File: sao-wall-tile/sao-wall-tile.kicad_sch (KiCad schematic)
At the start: 22 parts, among them J1 Power In, J2 Power Out, J3 Power Out, J4 Conn_02x03_Odd_Even, J5 Conn_02x03_Odd_Even, J6 Conn_02x03_Odd_Even, J7 Conn_02x03_Odd_Even, U1 LM2594M-3.3

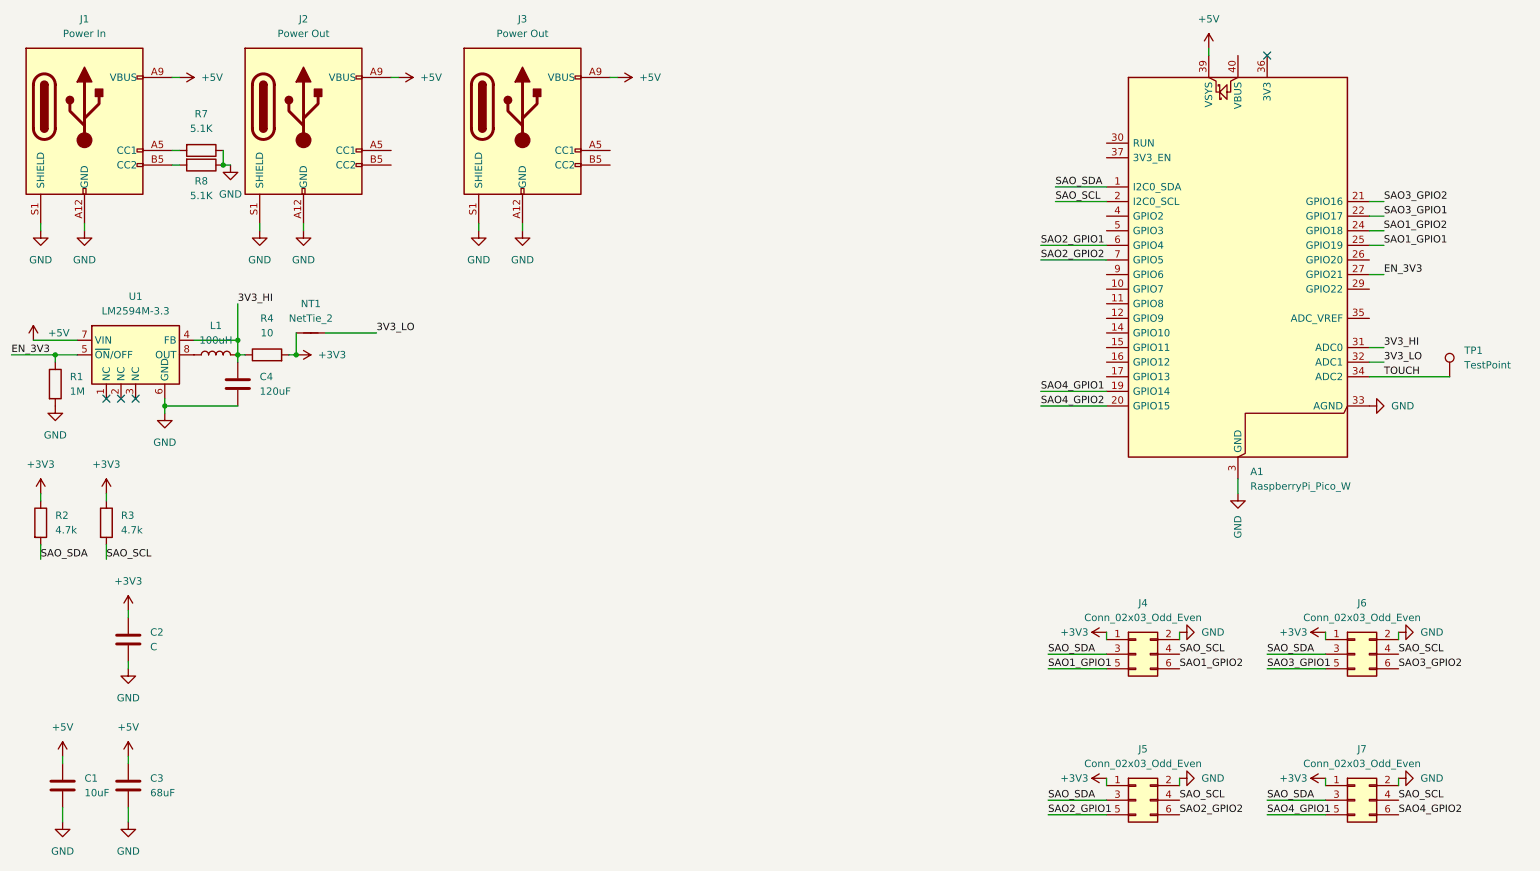
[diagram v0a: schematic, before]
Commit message: Add README, clean up schematic and layout
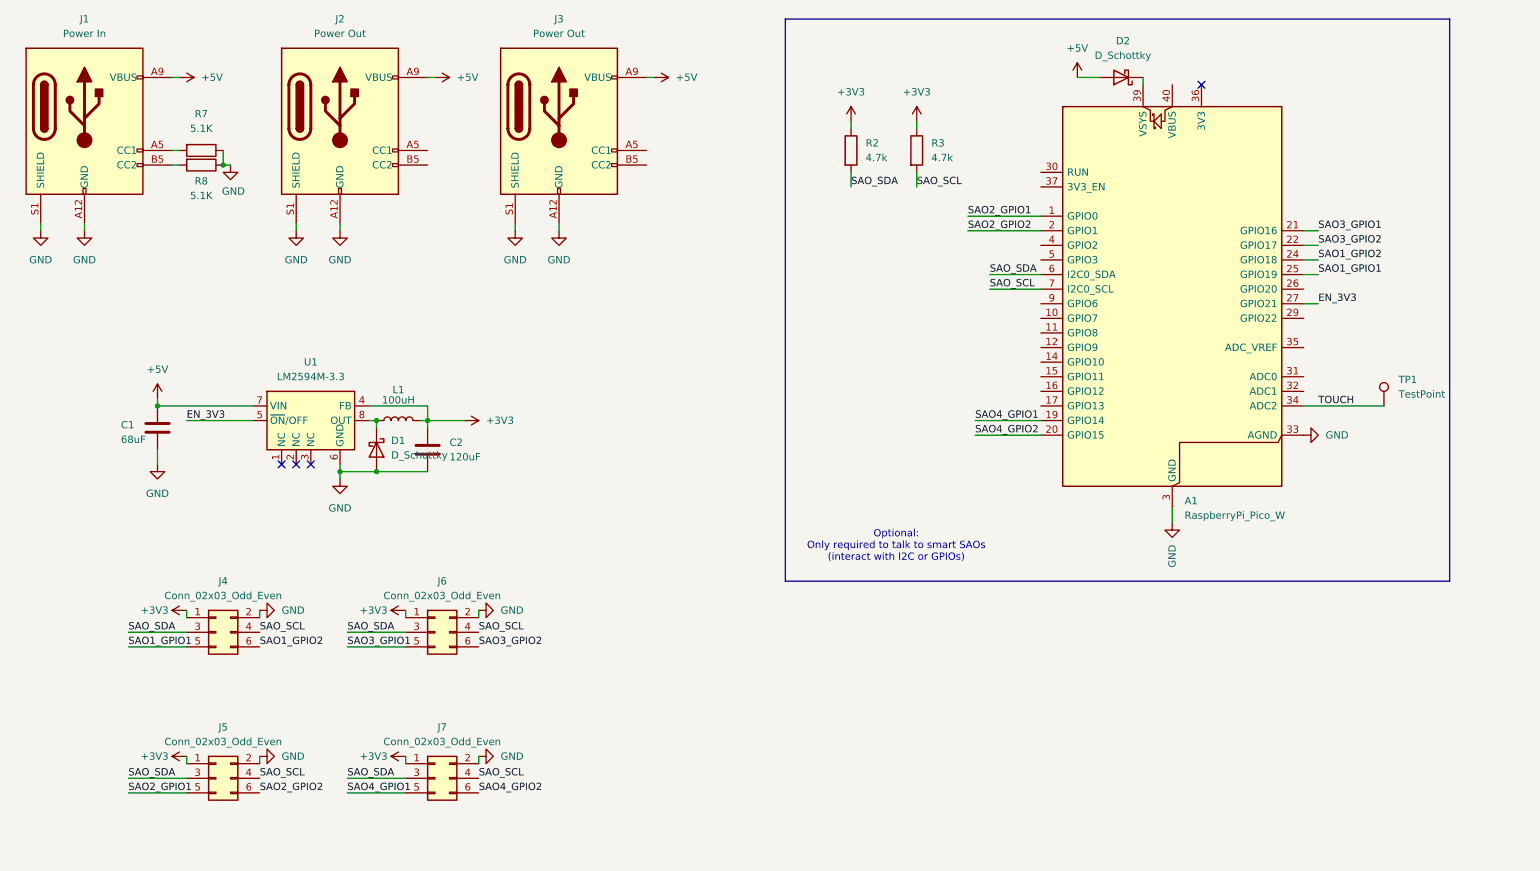
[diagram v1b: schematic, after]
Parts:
- removed C1: 10uF, Capacitor_SMD:C_0603_1608Metric, symbol Device:C
- removed C2: C, Capacitor_SMD:C_0603_1608Metric, symbol Device:C
- removed NT1: NetTie_2, NetTie:NetTie-2_SMD_Pad0.5mm, symbol Device:NetTie_2
- removed R1: 1M, Resistor_SMD:R_0603_1608Metric_Pad0.98x0.95mm_HandSolder, symbol Device:R
- removed R4: 10, Resistor_SMD:R_0603_1608Metric_Pad0.98x0.95mm_HandSolder, symbol Device:R
- added D1, D2: D_Schottky, Diode_SMD:D_0603_1608Metric_Pad1.05x0.95mm_HandSolder, symbol Device:D_Schottky
- renumbered C3 to C1, C4 to C2
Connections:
- net +3V3: now also C2.1, L1.2, U1.4 (FB)
- net +5V: now also D2.2 (A); no longer A1.39 (VSYS)
- net GND: now also D1.2 (A)
- net SAO2_GPIO1: now also A1.1 (GPIO0); no longer A1.6 (GPIO4)
- net SAO2_GPIO2: now also A1.2 (GPIO1); no longer A1.7 (GPIO5)
- net SAO3_GPIO1: now also A1.21 (GPIO16); no longer A1.22 (GPIO17)
- net SAO3_GPIO2: now also A1.22 (GPIO17); no longer A1.21 (GPIO16)
- net SAO_SCL: now also A1.7 (GPIO5); no longer A1.2 (GPIO1)
- net SAO_SDA: now also A1.6 (GPIO4); no longer A1.1 (GPIO0)
- net at L1.1, U1.8 (OUT): now also D1.1 (K)
- removed net 3V3_HI: A1.31 (GPIO26_ADC0), C2.1, L1.2, U1.4 (FB)
- net 3V3_LO: no longer names the net of A1.32 (GPIO27_ADC1)
- new net: A1.39 (VSYS), D2.1 (K)
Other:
- note added: "Optional: Only required to talk to smart SAOs (interact with I2C or GPIOs)"
- moved on the sheet: A1, C1, C2, J2, J3, J4, J5, J6, J7, L1, R2, R3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

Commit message: Update from review feedback
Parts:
- C1, C2: footprint Capacitor_SMD:C_0603_1608Metric -> Capacitor_SMD:C_0805_2012Metric_Pad1.18x1.45mm_HandSolder
- D1, D2: footprint Diode_SMD:D_0603_1608Metric_Pad1.05x0.95mm_HandSolder -> Diode_SMD:D_0805_2012Metric_Pad1.15x1.40mm_HandSolder
- L1: footprint Inductor_SMD:L_0603_1608Metric -> Inductor_SMD:L_0805_2012Metric_Pad1.05x1.20mm_HandSolder
- R2, R3, R7, R8: footprint Resistor_SMD:R_0603_1608Metric_Pad0.98x0.95mm_HandSolder -> Resistor_SMD:R_0805_2012Metric_Pad1.20x1.40mm_HandSolder
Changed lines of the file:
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@@
 	(wire
 		(pts
+			(xy 248.92 92.71) (xy 247.65 92.71)
+		)
+		(stroke
+			(width 0)
+			(type default)
+		)
+	)
+	(wire
+		(pts
 			(xy 86.36 99.06) (xy 95.25 99.06)
 		)
@@
 			)
 		)
-		(property "Footprint" "Resistor_SMD:R_0603_1608Metric_Pad0.98x0.95mm_HandSolder"
+		(property "Footprint" "Resistor_SMD:R_0805_2012Metric_Pad1.20x1.40mm_HandSolder"
 			(at 55.88 43.942 90)
 			(effects
@@
 			)
 		)
-		(property "Footprint" "Resistor_SMD:R_0603_1608Metric_Pad0.98x0.95mm_HandSolder"
+		(property "Footprint" "Resistor_SMD:R_0805_2012Metric_Pad1.20x1.40mm_HandSolder"
 			(at 178.562 43.18 90)
 			(effects
@@
 			)
 		)
-		(property "Footprint" "Capacitor_SMD:C_0603_1608Metric"
+		(property "Footprint" "Capacitor_SMD:C_0805_2012Metric_Pad1.18x1.45mm_HandSolder"
 			(at 49.2252 95.25 0)
 			(effects
@@
 			)
 		)
-		(property "Footprint" "Resistor_SMD:R_0603_1608Metric_Pad0.98x0.95mm_HandSolder"
+		(property "Footprint" "Resistor_SMD:R_0805_2012Metric_Pad1.20x1.40mm_HandSolder"
 			(at 167.132 43.18 90)
 			(effects
@@
 			)
 		)
-		(property "Footprint" "Inductor_SMD:L_0603_1608Metric"
+		(property "Footprint" "Inductor_SMD:L_0805_2012Metric_Pad1.05x1.20mm_HandSolder"
 			(at 90.17 90.17 0)
 			(effects
@@
 			)
 		)
-		(property "Footprint" "Diode_SMD:D_0603_1608Metric_Pad1.05x0.95mm_HandSolder"
+		(property "Footprint" "Diode_SMD:D_0805_2012Metric_Pad1.15x1.40mm_HandSolder"
 			(at 215.9 30.48 0)
 			(effects
@@
 			)
 		)
-		(property "Footprint" "Resistor_SMD:R_0603_1608Metric_Pad0.98x0.95mm_HandSolder"
+		(property "Footprint" "Resistor_SMD:R_0805_2012Metric_Pad1.20x1.40mm_HandSolder"
 			(at 55.88 41.402 90)
 			(effects
@@
 	(symbol
 		(lib_id "power:GND")
-		(at 247.65 92.71 90)
+		(at 248.92 92.71 90)
 		(unit 1)
 		(exclude_from_sim no)
@@
 		(dnp no)
 		(property "Reference" "#PWR016"
-			(at 254 92.71 0)
+			(at 255.27 92.71 0)
 			(effects
 				(font
@@
 		)
 		(property "Value" "GND"
-			(at 251.46 92.7101 90)
+			(at 252.73 92.7101 90)
 			(effects
 				(font
@@
 		)
 		(property "Footprint" ""
-			(at 247.65 92.71 0)
+			(at 248.92 92.71 0)
 			(effects
 				(font
@@
 		)
 		(property "Datasheet" ""
-			(at 247.65 92.71 0)
+			(at 248.92 92.71 0)
 			(effects
 				(font
@@
 		)
 		(property "Description" "Power symbol creates a global label with name \"GND\" , ground"
-			(at 247.65 92.71 0)
+			(at 248.92 92.71 0)
 			(effects
 				(font
@@
 			)
 		)
-		(property "Footprint" "Capacitor_SMD:C_0603_1608Metric"
+		(property "Footprint" "Capacitor_SMD:C_0805_2012Metric_Pad1.18x1.45mm_HandSolder"
 			(at 96.2152 99.06 0)
 			(effects
@@
 			)
 		)
-		(property "Footprint" "Diode_SMD:D_0603_1608Metric_Pad1.05x0.95mm_HandSolder"
+		(property "Footprint" "Diode_SMD:D_0805_2012Metric_Pad1.15x1.40mm_HandSolder"
 			(at 86.36 95.25 0)
 			(effects

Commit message: Updates from picking components on digikey
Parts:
- C1: footprint Capacitor_SMD:C_0805_2012Metric_Pad1.18x1.45mm_HandSolder -> Capacitor_SMD:C_Elec_5x5.8
- C2: footprint Capacitor_SMD:C_0805_2012Metric_Pad1.18x1.45mm_HandSolder -> Capacitor_SMD:C_Elec_8x10.2
- D1: footprint Diode_SMD:D_0805_2012Metric_Pad1.15x1.40mm_HandSolder -> Diode_SMD:D_SOD-123
- L1: value 100uH -> 47uH; footprint Inductor_SMD:L_0805_2012Metric_Pad1.05x1.20mm_HandSolder -> Inductor_SMD:L_Taiyo-Yuden_NR-60xx_HandSoldering
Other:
- moved on the sheet: C2
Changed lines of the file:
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@@
 	)
 	(junction
-		(at 86.36 90.17)
+		(at 102.87 90.17)
 		(diameter 0)
 		(color 0 0 0 0)
 	)
 	(junction
-		(at 48.26 87.63)
+		(at 86.36 90.17)
 		(diameter 0)
 		(color 0 0 0 0)
 	)
 	(junction
-		(at 95.25 90.17)
+		(at 48.26 87.63)
 		(diameter 0)
 		(color 0 0 0 0)
@@
 	(wire
 		(pts
-			(xy 86.36 99.06) (xy 95.25 99.06)
+			(xy 86.36 99.06) (xy 102.87 99.06)
 		)
 		(stroke
@@
 	(wire
 		(pts
-			(xy 95.25 87.63) (xy 95.25 90.17)
+			(xy 102.87 87.63) (xy 102.87 90.17)
 		)
 		(stroke
@@
 	(wire
 		(pts
-			(xy 95.25 90.17) (xy 93.98 90.17)
+			(xy 102.87 90.17) (xy 93.98 90.17)
 		)
 		(stroke
@@
 	(wire
 		(pts
-			(xy 95.25 91.44) (xy 95.25 90.17)
+			(xy 102.87 91.44) (xy 102.87 90.17)
 		)
 		(stroke
@@
 	(wire
 		(pts
-			(xy 85.09 87.63) (xy 95.25 87.63)
+			(xy 85.09 87.63) (xy 102.87 87.63)
 		)
 		(stroke
@@
 	(wire
 		(pts
-			(xy 101.6 90.17) (xy 95.25 90.17)
+			(xy 110.49 90.17) (xy 102.87 90.17)
 		)
 		(stroke
@@
 	(symbol
 		(lib_id "power:VCC")
-		(at 101.6 90.17 270)
+		(at 110.49 90.17 270)
 		(unit 1)
 		(exclude_from_sim no)
@@
 		(fields_autoplaced yes)
 		(property "Reference" "#PWR025"
-			(at 97.79 90.17 0)
+			(at 106.68 90.17 0)
 			(effects
 				(font
@@
 		)
 		(property "Value" "+3V3"
-			(at 105.41 90.1699 90)
+			(at 114.3 90.1699 90)
 			(effects
 				(font
@@
 		)
 		(property "Footprint" ""
-			(at 101.6 90.17 0)
+			(at 110.49 90.17 0)
 			(effects
 				(font
@@
 		)
 		(property "Datasheet" ""
-			(at 101.6 90.17 0)
+			(at 110.49 90.17 0)
 			(effects
 				(font
@@
 		)
 		(property "Description" "Power symbol creates a global label with name \"VCC\""
-			(at 101.6 90.17 0)
+			(at 110.49 90.17 0)
 			(effects
 				(font
@@
 			)
 		)
-		(property "Footprint" "Capacitor_SMD:C_0805_2012Metric_Pad1.18x1.45mm_HandSolder"
+		(property "Footprint" "Capacitor_SMD:C_Elec_5x5.8"
 			(at 49.2252 95.25 0)
 			(effects
@@
 			)
 		)
-		(property "Value" "100uH"
+		(property "Value" "47uH"
 			(at 90.17 86.614 90)
 			(effects
@@
 			)
 		)
-		(property "Footprint" "Inductor_SMD:L_0805_2012Metric_Pad1.05x1.20mm_HandSolder"
+		(property "Footprint" "Inductor_SMD:L_Taiyo-Yuden_NR-60xx_HandSoldering"
 			(at 90.17 90.17 0)
 			(effects
@@
 	(symbol
 		(lib_id "Device:C")
-		(at 95.25 95.25 0)
+		(at 102.87 95.25 0)
 		(unit 1)
 		(exclude_from_sim no)
@@
 		(fields_autoplaced yes)
 		(property "Reference" "C2"
-			(at 99.06 93.9799 0)
+			(at 106.68 93.9799 0)
 			(effects
 				(font
@@
 		)
 		(property "Value" "120uF"
-			(at 99.06 96.5199 0)
+			(at 106.68 96.5199 0)
 			(effects
 				(font
@@
 			)
 		)
-		(property "Footprint" "Capacitor_SMD:C_0805_2012Metric_Pad1.18x1.45mm_HandSolder"
-			(at 96.2152 99.06 0)
+		(property "Footprint" "Capacitor_SMD:C_Elec_8x10.2"
+			(at 103.8352 99.06 0)
 			(effects
 				(font
@@
 		)
 		(property "Datasheet" "~"
-			(at 95.25 95.25 0)
+			(at 102.87 95.25 0)
 			(effects
 				(font
@@
 		)
 		(property "Description" "Unpolarized capacitor"
-			(at 95.25 95.25 0)
+			(at 102.87 95.25 0)
 			(effects
 				(font
@@
 			)
 		)
-		(property "Footprint" "Diode_SMD:D_0805_2012Metric_Pad1.15x1.40mm_HandSolder"
+		(property "Footprint" "Diode_SMD:D_SOD-123"
 			(at 86.36 95.25 0)
 			(effects

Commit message: Made C2 smaller
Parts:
- C2: footprint Capacitor_SMD:C_Elec_8x10.2 -> Capacitor_SMD:C_Elec_6.3x7.7
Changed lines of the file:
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@@
 			)
 		)
-		(property "Footprint" "Capacitor_SMD:C_Elec_8x10.2"
+		(property "Footprint" "Capacitor_SMD:C_Elec_6.3x7.7"
 			(at 103.8352 99.06 0)
 			(effects

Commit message: Different buck converter for smaller and cheaper components
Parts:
- removed D1: D_Schottky, Diode_SMD:D_SOD-123, symbol Device:D_Schottky
- removed U1: LM2594M-3.3, Package_SO:SOIC-8_3.9x4.9mm_P1.27mm, symbol Regulator_Switching:LM2594M-3.3
- added R1: 1M, Resistor_SMD:R_0805_2012Metric_Pad1.20x1.40mm_HandSolder, symbol Device:R
- added U1: ~, Package_TO_SOT_SMD:TSOT-23-5_HandSoldering, symbol ben_custom:MCP1603BT-330I/OS
- C1: value 68uF -> 4.7uF; footprint Capacitor_SMD:C_Elec_5x5.8 -> Capacitor_SMD:C_0805_2012Metric_Pad1.18x1.45mm_HandSolder
- C2: value 120uF -> 4.7uF; footprint Capacitor_SMD:C_Elec_6.3x7.7 -> Capacitor_SMD:C_0805_2012Metric_Pad1.18x1.45mm_HandSolder
- L1: value 47uH -> 4.7uH; footprint Inductor_SMD:L_Taiyo-Yuden_NR-60xx_HandSoldering -> Inductor_SMD:L_1008_2520Metric_Pad1.43x2.20mm_HandSolder
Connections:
- net +3V3: now also U1.4 (VFB)
- net +5V: now also R1.2, U1.1 (VIN)
- net EN_3V3: now also R1.1, U1.3 (SHDN)
- net GND: now also U1.2 (GND)
- net at L1.1: now also U1.5 (Lx)
- no-connect marks 4 -> 1

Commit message: Move GPIO pins, update from more review, enhance labels, update renders
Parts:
- renumbered R7 to R4, R8 to R5
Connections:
- net SAO4_GPIO1: now also A1.11 (GPIO8); no longer A1.19 (GPIO14)
- net SAO4_GPIO2: now also A1.12 (GPIO9); no longer A1.20 (GPIO15)
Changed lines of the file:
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@@
 	(wire
 		(pts
-			(xy 190.5 90.17) (xy 201.93 90.17)
-		)
-		(stroke
-			(width 0)
-			(type default)
-		)
-	)
-	(wire
-		(pts
 			(xy 247.65 64.77) (xy 250.19 64.77)
 		)
@@
 	(wire
 		(pts
-			(xy 190.5 92.71) (xy 201.93 92.71)
-		)
-		(stroke
-			(width 0)
-			(type default)
-		)
-	)
-	(wire
-		(pts
 			(xy 91.44 148.59) (xy 91.44 149.86)
 		)
@@
 	(wire
 		(pts
+			(xy 189.23 74.93) (xy 201.93 74.93)
+		)
+		(stroke
+			(width 0)
+			(type default)
+		)
+	)
+	(wire
+		(pts
 			(xy 189.23 54.61) (xy 201.93 54.61)
 		)
@@
 	(wire
 		(pts
+			(xy 189.23 77.47) (xy 201.93 77.47)
+		)
+		(stroke
+			(width 0)
+			(type default)
+		)
+	)
+	(wire
+		(pts
 			(xy 247.65 87.63) (xy 261.62 87.63)
 		)
@@
 		)
 	)
+	(label "SAO4_GPIO1"
+		(at 189.23 74.93 0)
+		(effects
+			(font
+				(size 1.27 1.27)
+			)
+			(justify left bottom)
+		)
+	)
 	(label "SAO4_GPIO2"
-		(at 190.5 92.71 0)
+		(at 189.23 77.47 0)
 		(effects
 			(font
@@
 		)
 	)
-	(label "SAO4_GPIO1"
-		(at 190.5 90.17 0)
-		(effects
-			(font
-				(size 1.27 1.27)
-			)
-			(justify left bottom)
-		)
-	)
 	(label "SAO1_GPIO1"
 		(at 250.19 64.77 0)
@@
 		(on_board yes)
 		(dnp no)
-		(property "Reference" "R8"
+		(property "Reference" "R5"
 			(at 55.88 48.514 90)
 			(effects
@@
 			(project ""
 				(path "/1b373ada-da4c-41cd-a895-48eab357c8f4"
-					(reference "R8")
+					(reference "R5")
 					(unit 1)
 				)
@@
 		(dnp no)
 		(fields_autoplaced yes)
-		(property "Reference" "R7"
+		(property "Reference" "R4"
 			(at 55.88 36.83 90)
 			(effects
@@
 			(project ""
 				(path "/1b373ada-da4c-41cd-a895-48eab357c8f4"
-					(reference "R7")
+					(reference "R4")
 					(unit 1)
 				)
